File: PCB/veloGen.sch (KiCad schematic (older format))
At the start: 24 parts, among them J1 Conn_01x06, J2 Gen. IN, J3 Bat, U1 ESP-WROOM-32, U2 TS1101, U4 MAX8881

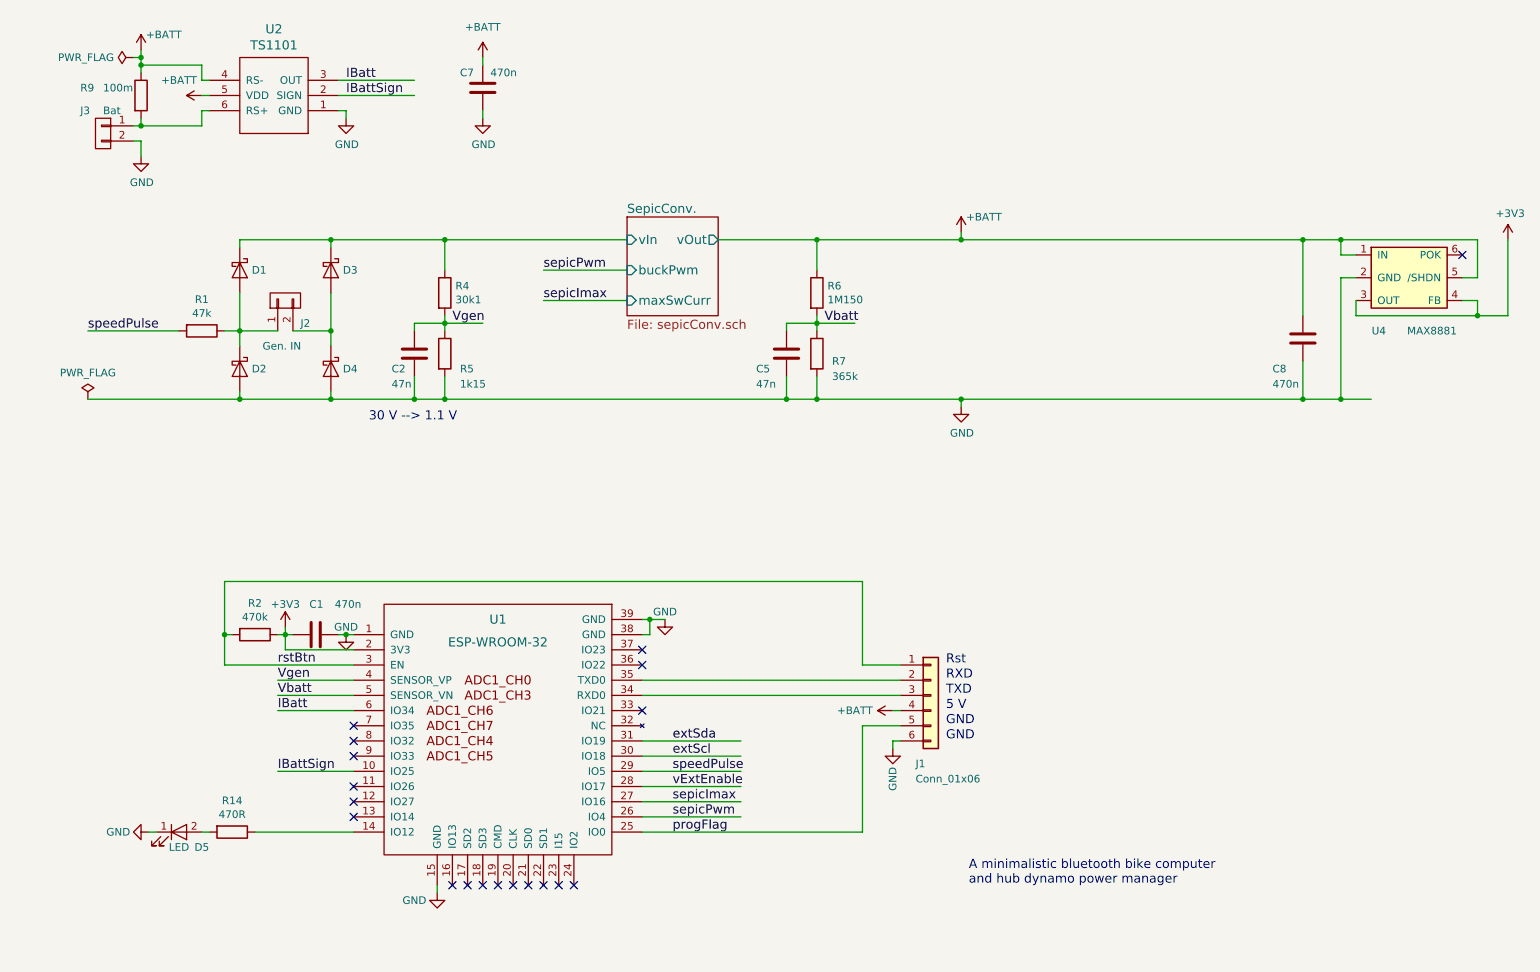
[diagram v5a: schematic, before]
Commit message: moved stuff around 0.6 vias
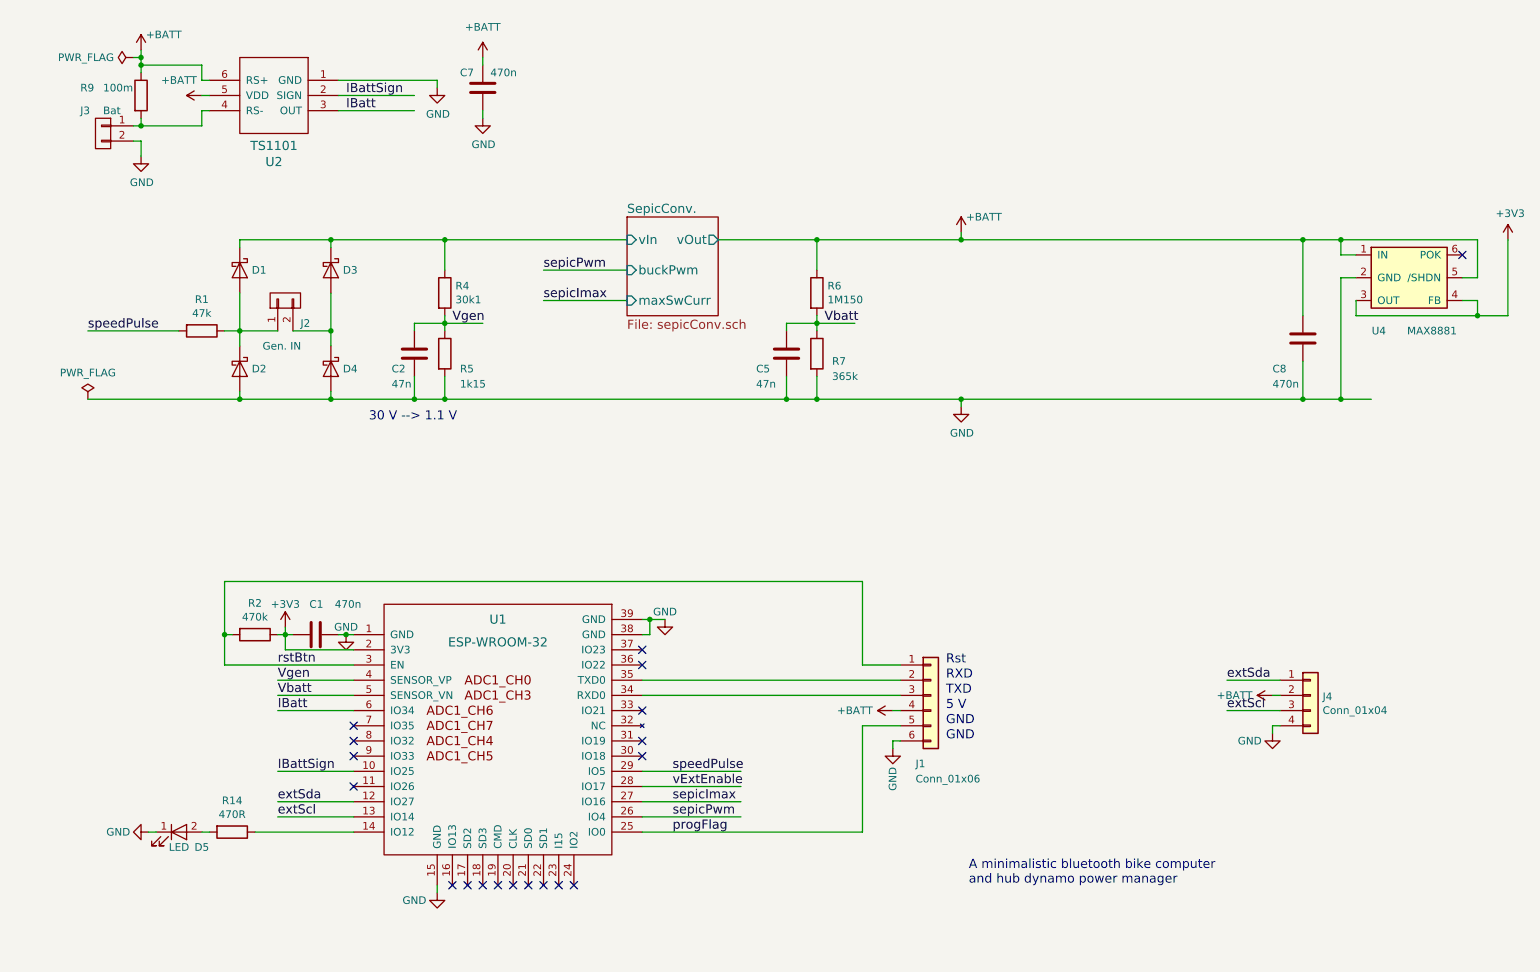
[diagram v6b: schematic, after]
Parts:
- added J4: Conn_01x04, Socket_Strips:Socket_Strip_Straight_1x04_Pitch2.54mm, symbol Conn_01x04
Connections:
- wire segments 94 -> 99

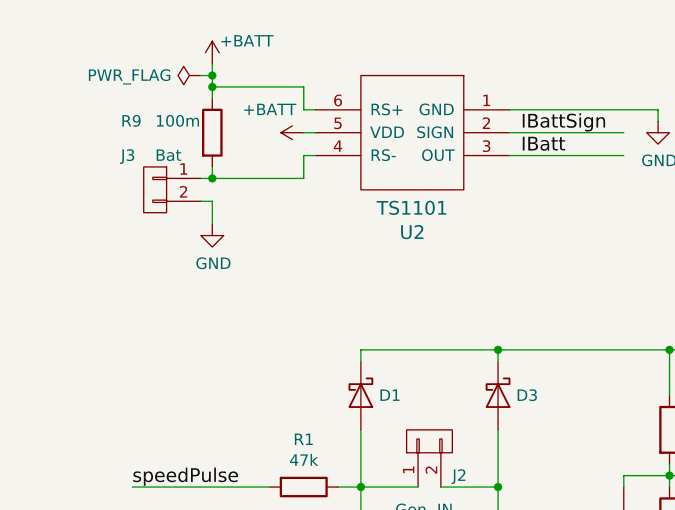
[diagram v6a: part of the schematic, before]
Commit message: built first prototype, some mods are needed
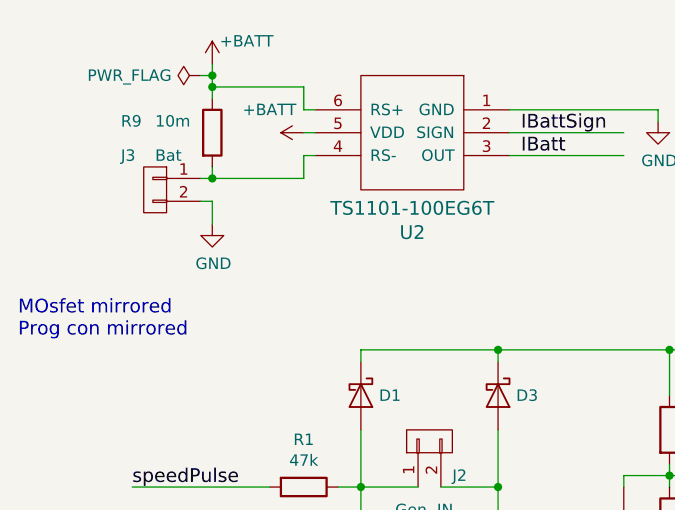
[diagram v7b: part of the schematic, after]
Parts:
- R9: value 100m -> 10m
- U2: value TS1101 -> TS1101-100EG6T
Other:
- note added: "MOsfet mirrored\nProg con mirrored"
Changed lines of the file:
@@
-EESchema Schematic File Version 2
+EESchema Schematic File Version 3
 LIBS:veloGen-rescue
 LIBS:power
@@
 LIBS:contrib
 LIBS:valves
-LIBS:myStuff
 LIBS:veloGen-cache
 EELAYER 26 0
@@
 P 2850 1650
 F 0 "U2" H 3225 1313 60  0000 C CNN
-F 1 "TS1101" H 3225 1419 60  0000 C CNN
+F 1 "TS1101-100EG6T" H 3225 1419 60  0000 C CNN
 F 2 "TO_SOT_Packages_SMD:SOT-23-6_Handsoldering" H 3250 1250 60  0001 C CNN
 F 3 "https://www.silabs.com/documents/public/data-sheets/TS1100-01-02-03.pdf" H 4000 1400 60  0001 C CNN
@@
 P 1600 1550
 F 0 "R9" H 1200 1600 50  0000 L CNN
-F 1 "100m" H 1350 1600 50  0000 L CNN
+F 1 "10m" H 1350 1600 50  0000 L CNN
 F 2 "Resistors_SMD:R_1206" V 1530 1550 50  0001 C CNN
 F 3 "" H 1600 1550 50  0001 C CNN
@@
 Text Label 8750 5600 0    60   ~ 0
 extScl
+Text Notes 750  2450 0    60   ~ 0
+MOsfet mirrored\nProg con mirrored
 $EndSCHEMATC

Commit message: Cleaned up a bit
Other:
- note added: "MOsfet mirrored\nProg con mirrored\n3.3 reg to wimpy"
- note removed: "MOsfet mirrored\nProg con mirrored"
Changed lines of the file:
@@
 extScl
 Text Notes 750  2450 0    60   ~ 0
-MOsfet mirrored\nProg con mirrored
+MOsfet mirrored\nProg con mirrored\n3.3 reg to wimpy
 $EndSCHEMATC
